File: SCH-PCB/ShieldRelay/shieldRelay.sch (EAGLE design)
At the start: 54 parts, among them IC1 LM2596SX-5.0_NOPB, K1 SLA-05VDC-SL-C, K2 SRD-05VDC-SL-C, K3 G3MB-202PL-DC5, K5 G3MB-202PL-DC5, K6 SRD-05VDC-SL-C, Q1 MMST2222A-7-F, Q2 MMST2222A-7-F, Q3 MMST2222A-7-F, Q4 MMST2222A-7-F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

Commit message: FEAT: Positioning component
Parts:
- removed NODE1: NODEMCU_ESP8266, nodemcu_esp8266:NODEMCU_ESP8266
- added INPUT: 1759017, 1759017:1759017
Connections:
- net GND: now also INPUT.2
- net VCC: now also INPUT.1
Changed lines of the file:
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@@
 <part name="FRAME1" library="frames" library_urn="urn:adsk.eagle:library:229" deviceset="A4L-LOC" device=""/>
 <part name="BOARD1" library="ESP32-DEVKITV1" deviceset="ESP32DEVKITV1" device=""/>
-<part name="NODE1" library="nodemcu_esp8266" deviceset="NODEMCU_ESP8266" device=""/>
 <part name="K1" library="SLA-05VDC-SL-C" deviceset="SLA-05VDC-SL-C" device=""/>
 <part name="K2" library="SRD-05VDC-SL-C" deviceset="SRD-05VDC-SL-C" device=""/>
@@
 <part name="P+9" library="supply1" library_urn="urn:adsk.eagle:library:371" deviceset="VCC/2" device=""/>
 <part name="P+10" library="supply1" library_urn="urn:adsk.eagle:library:371" deviceset="VCC/2" device=""/>
+<part name="INPUT" library="1759017" deviceset="1759017" device=""/>
+<part name="P+11" library="supply1" library_urn="urn:adsk.eagle:library:371" deviceset="VCC" device=""/>
+<part name="GND9" library="supply1" library_urn="urn:adsk.eagle:library:371" deviceset="GND" device=""/>
 </parts>
 <sheets>
@@
 <attribute name="NAME" x="450.723" y="110.363" size="1.27" layer="95" rot="R180"/>
 </instance>
-<instance part="NODE1" gate="G$1" x="512.318" y="143.51" smashed="yes">
-<attribute name="VALUE" x="502.158" y="115.57" size="1.27" layer="96"/>
-<attribute name="NAME" x="502.158" y="161.29" size="1.27" layer="95"/>
-</instance>
 <instance part="K1" gate="G$1" x="78.994" y="119.634" smashed="yes" rot="R90">
 <attribute name="NAME" x="75.184" y="138.43" size="1.016" layer="95" rot="R90" align="center-left"/>
@@
 <instance part="P+10" gate="G$1" x="397.256" y="69.596" smashed="yes" rot="R180">
 <attribute name="VALUE" x="394.716" y="66.294" size="1.016" layer="96"/>
+</instance>
+<instance part="INPUT" gate="G$1" x="289.56" y="136.144" smashed="yes" rot="R270">
+<attribute name="NAME" x="286.512" y="119.888" size="1.016" layer="95" align="center-left"/>
+</instance>
+<instance part="P+11" gate="VCC" x="289.56" y="140.716" smashed="yes">
+<attribute name="VALUE" x="291.084" y="142.494" size="1.016" layer="96" rot="R180"/>
+</instance>
+<instance part="GND9" gate="1" x="287.02" y="139.446" smashed="yes" rot="R180">
+<attribute name="VALUE" x="288.544" y="140.97" size="1.016" layer="96" rot="R180"/>
 </instance>
 </instances>
@@
 <junction x="444.5" y="79.756"/>
 </segment>
+<segment>
+<pinref part="GND9" gate="1" pin="GND"/>
+<pinref part="INPUT" gate="G$1" pin="2"/>
+<wire x1="287.02" y1="136.906" x2="287.02" y2="136.144" width="0.1524" layer="91"/>
+</segment>
 </net>
 <net name="IN2" class="0">
@@
 <wire x1="280.67" y1="155.194" x2="281.94" y2="155.194" width="0.1524" layer="91"/>
 </segment>
-</net>
+<segment>
+<pinref part="P+11" gate="VCC" pin="VCC"/>
+<pinref part="INPUT" gate="G$1" pin="1"/>
+<wire x1="289.56" y1="138.176" x2="289.56" y2="136.144" width="0.1524" layer="91"/>
+</segment>
+</net>

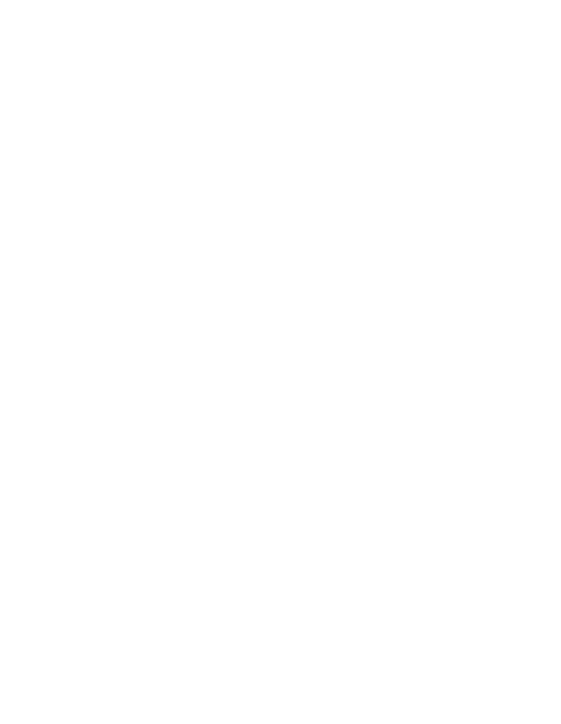
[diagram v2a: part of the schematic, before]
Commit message: FEAT: update library pinhead
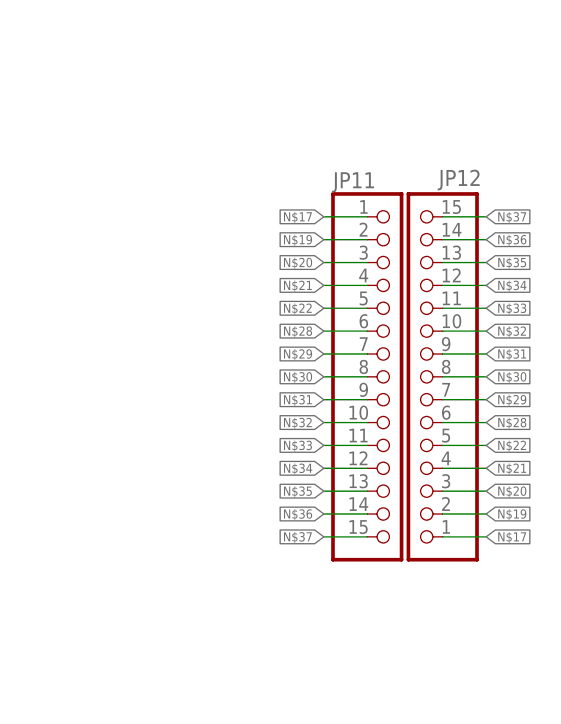
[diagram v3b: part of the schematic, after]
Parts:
- added JP11, JP12: (no value), pinhead_mod:PINHD-1X15
- JP1, JP2, JP3, JP4, JP5, JP6: device pinhead:PINHD-1X15 -> pinhead_mod:PINHD-1X15
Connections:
- net N$17: now also JP11.1, JP12.1
- net N$19: now also JP11.2, JP12.2
- net N$20: now also JP11.3, JP12.3
- net N$21: now also JP11.4, JP12.4
- net N$22: now also JP11.5, JP12.5
- net N$28: now also JP11.6, JP12.6
- net N$29: now also JP11.7, JP12.7
- net N$30: now also JP11.8, JP12.8
- net N$31: now also JP11.9, JP12.9
- net N$32: now also JP11.10, JP12.10
- net N$33: now also JP11.11, JP12.11
- net N$34: now also JP11.12, JP12.12
- net N$35: now also JP11.13, JP12.13
- net N$36: now also JP11.14, JP12.14
- net N$37: now also JP11.15, JP12.15
